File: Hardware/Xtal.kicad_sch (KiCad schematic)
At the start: 3 parts, among them Y1 16MHz

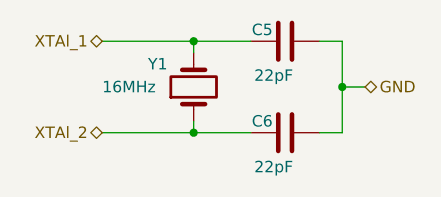
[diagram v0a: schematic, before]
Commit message: Update PCB of Motor controller - version sent on production (debug purpose)
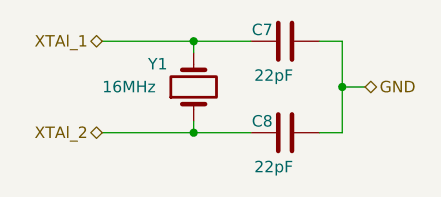
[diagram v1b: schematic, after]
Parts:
- renumbered C5 to C7, C6 to C8
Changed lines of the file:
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@@
 		(on_board yes)
 		(dnp no)
-		(property "Reference" "C5"
+		(property "Reference" "C7"
 			(at 93.98 69.85 90)
 			(effects
@@
 			(project "Tracker"
 				(path "/60c5e70b-bc37-4402-aa86-9378cecb8f85/9d930418-4d94-42d8-8741-e1ee0e746f35"
-					(reference "C5")
+					(reference "C7")
 					(unit 1)
 				)
@@
 		(on_board yes)
 		(dnp no)
-		(property "Reference" "C6"
+		(property "Reference" "C8"
 			(at 93.98 80.01 90)
 			(effects
@@
 			(project "Tracker"
 				(path "/60c5e70b-bc37-4402-aa86-9378cecb8f85/9d930418-4d94-42d8-8741-e1ee0e746f35"
-					(reference "C6")
+					(reference "C8")
 					(unit 1)
 				)
